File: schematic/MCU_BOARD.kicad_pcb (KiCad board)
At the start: 2 copper layers, 79.2 x 101.1 mm, 83 parts, among them J2 Speaker_Conn_01x02, J3 Barrel_Jack_Switch, J4 Conn_01x27, Q1 2N3904, Q2 2N3904, Q3 2N3904, Q4 2N3904, Q5 2N3904, U5 LM386, U6 74HC4051, U7 AT89S51-24PU, U9 SN74HC4060N, Y1 32.768Khz, Y2 12Mhz

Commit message: bad state, but wanted to document changes to the v1 cap values. Need to fix PCB, it got messed up for some odd reason.
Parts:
- removed H3: MountingHole, MountingHole:MountingHole_3.2mm_M3
- removed J4: Conn_01x27, Connector_PinHeader_2.54mm:PinHeader_1x27_P2.54mm_Vertical
- removed R42, R43: 100R, Resistor_THT:R_Axial_DIN0207_L6.3mm_D2.5mm_P7.62mm_Horizontal
- removed U5: LM386, Package_DIP:DIP-8_W7.62mm_LongPads
- removed U7: AT89S51-24PU, AT89S51-33PU:DIP1556W56P254L5232H483Q40N
- removed U9: SN74HC4060N, Package_DIP:DIP-16_W7.62mm_LongPads
- added H1: MountingHole, MountingHole:MountingHole_3.2mm_M3, F.Cu at (187.8, 36.1)
- added IC1: SN74HC4060N, Package_DIP:DIP-16_W7.62mm_LongPads, F.Cu at (189.5, 45.0)
- added IC2: AT89S51-24PU, AT89S51-33PU:DIP1556W56P254L5232H483Q40N, F.Cu at (147.9, 87.4)
- added J1: Speaker_Conn_01x02, Connector_Molex:Molex_KK-254_AE-6410-02A_1x02_P2.54mm_Vertical, F.Cu at (154.4, 50.9)
- added R1: 4k7, Resistor_THT:R_Axial_DIN0207_L6.3mm_D2.5mm_P7.62mm_Horizontal, F.Cu at (198.9, 70.6)
- added R2: 4k7, Resistor_THT:R_Axial_DIN0207_L6.3mm_D2.5mm_P7.62mm_Horizontal, F.Cu at (171.2, 103.1)
- added U1: LM386, Package_DIP:DIP-8_W7.62mm_LongPads, F.Cu at (142.2, 39.1)
- C1: footprint Capacitor_THT:C_Disc_D4.3mm_W1.9mm_P5.00mm -> Capacitor_THT:C_Disc_D3.0mm_W1.6mm_P2.50mm
- C13: value 4.7uF -> 2uF
- C14: value 47nF -> 47pF; footprint Capacitor_THT:C_Disc_D4.3mm_W1.9mm_P5.00mm -> Capacitor_THT:C_Disc_D3.0mm_W2.0mm_P2.50mm
- C15: value 330uF -> 220uF; footprint Capacitor_THT:CP_Radial_D6.3mm_P2.50mm -> Capacitor_THT:CP_Radial_D10.0mm_P5.00mm_P7.50mm
- C16: value 330uF -> 470uF; footprint Capacitor_THT:CP_Radial_D6.3mm_P2.50mm -> Capacitor_THT:CP_Radial_D10.0mm_P5.00mm_P7.50mm
- C2: value 6-30pF -> 2-5pF; footprint Capacitor_THT:C_Rect_L7.0mm_W6.5mm_P5.00mm -> Capacitor_THT:C_Rect_L10.0mm_W5.0mm_P5.00mm_P7.50mm
- C24: value 10uF -> 2.2uF
- C26: value 18pF -> 10pF
- J2: value Speaker_Conn_01x02 -> Barrel_Jack_Switch; footprint Connector_Molex:Molex_KK-254_AE-6410-02A_1x02_P2.54mm_Vertical -> Connector_BarrelJack:BarrelJack_Horizontal
- J3: value Barrel_Jack_Switch -> Conn_01x27; footprint Connector_BarrelJack:BarrelJack_Horizontal -> Connector_PinHeader_2.54mm:PinHeader_1x27_P2.54mm_Vertical
- R13: value 470R -> 10M
- R14: value 470R -> 270R
- R15: value 10M -> 10K
- R16: value 1K -> 1k
- R17: value 10K -> 8R_OPT; footprint Resistor_THT:R_Axial_DIN0207_L6.3mm_D2.5mm_P7.62mm_Horizontal -> Resistor_THT:R_Axial_DIN0414_L11.9mm_D4.5mm_P15.24mm_Horizontal
- R18: value 1k -> 5K
- R19: value 8R_OPT -> 500R; footprint Resistor_THT:R_Axial_DIN0414_L11.9mm_D4.5mm_P15.24mm_Horizontal -> Resistor_THT:R_Axial_DIN0207_L6.3mm_D2.5mm_P7.62mm_Horizontal
- R20: value 10K -> 270R; footprint Resistor_THT:R_Axial_DIN0207_L6.3mm_D2.5mm_P7.62mm_Horizontal -> Resistor_THT:R_Axial_DIN0207_L6.3mm_D2.5mm_P10.16mm_Horizontal
- R21: value 470R -> 270R; footprint Resistor_THT:R_Axial_DIN0207_L6.3mm_D2.5mm_P7.62mm_Horizontal -> Resistor_THT:R_Axial_DIN0207_L6.3mm_D2.5mm_P10.16mm_Horizontal
- R22, R23, R24, R25: value 1K -> 270R
- R26: value 1K -> 10R; footprint Resistor_THT:R_Axial_DIN0207_L6.3mm_D2.5mm_P10.16mm_Horizontal -> Resistor_THT:R_Axial_DIN0207_L6.3mm_D2.5mm_P7.62mm_Horizontal
- R27: value 1K -> 10K; footprint Resistor_THT:R_Axial_DIN0207_L6.3mm_D2.5mm_P10.16mm_Horizontal -> Resistor_THT:R_Axial_DIN0207_L6.3mm_D2.5mm_P7.62mm_Horizontal
- R28: value 10R -> 1k
- R35: value 10K -> 100R
- R36: value 1k -> 100R
- R6: value 4k7 -> 1k
- R7: value 4k7 -> 1M
- R8: value 1k -> 470R
- R9: value 200k -> 470R
- moved J3 81.4 mm to (124.3, 125.0), turned to 90 degrees
- moved R27 40.5 mm to (221.8, 97.6)
- moved R26 34.5 mm to (215.9, 101.7)
- moved J2 30.6 mm to (124.5, 43.5), turned to -90 degrees
- moved R8 11.4 mm to (191.5, 66.8)
- moved C15 0.09 mm to (142.3, 51.9)
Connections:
- C1 pad 2: Net-(C1-Pad2) -> Net-(IC1-CLKI)
- C10 pad 1: Net-(C10-Pad1) -> Net-(U1-+)
- C20 pad 2: Net-(C20-Pad2) -> Net-(IC1-~{CLKO})
- C3 pad 2: Net-(C3-Pad2) -> Net-(IC1-CLR)
- C4 pad 1: Net-(C4-Pad1) -> Net-(IC2-(RXD)_P3.0)
- C5 pad 1: Net-(C5-Pad1) -> Net-(IC2-(TXD)_P3.1)
- C6 pad 1: Net-(C6-Pad1) -> Net-(IC2-(~{INT0})_P3.2)
- C7 pad 1: Net-(C7-Pad1) -> Net-(IC2-(~{INT1})_P3.3)
- C8 pad 1: Net-(C8-Pad1) -> Net-(IC2-(T0)_P3.4)
- J2 pad 1: GND -> VCC
- J2 pad 2: Net-(J2-Pad2) -> GND
- J3 pad 1: VCC -> /AL
- J3 pad 2: GND -> /B
- J3 pad 3: GND -> /A
- Q1 pad 2: Net-(Q1-Pad2) -> Net-(Q1-B)
- Q1 pad 3: /LED_DISPLAY_BOARD/DL -> /DL
- Q2 pad 2: Net-(Q2-Pad2) -> Net-(Q2-B)
- Q2 pad 3: /LED_DISPLAY_BOARD/TEN_H -> /TEN_H
- Q3 pad 2: Net-(Q3-Pad2) -> Net-(Q3-B)
- Q3 pad 3: /LED_DISPLAY_BOARD/ONE_H -> /ONE_H
- Q4 pad 2: Net-(Q4-Pad2) -> Net-(Q4-B)
- Q4 pad 3: /LED_DISPLAY_BOARD/TEN_M -> /TEN_M
- Q5 pad 2: Net-(Q5-Pad2) -> Net-(Q5-B)
- Q5 pad 3: /LED_DISPLAY_BOARD/ONE_M -> /ONE_M
- R10 pad 1: /LED_DISPLAY_BOARD/HS -> /AS
- R10 pad 2: Net-(C4-Pad1) -> Net-(IC2-(~{INT0})_P3.2)
- R11 pad 1: Net-(C5-Pad1) -> /TS
- R11 pad 2: /LED_DISPLAY_BOARD/MS -> Net-(IC2-(~{INT1})_P3.3)
- R12 pad 1: /LED_DISPLAY_BOARD/AS -> /SAS
- R12 pad 2: Net-(C6-Pad1) -> Net-(IC2-(T0)_P3.4)
- R13 pad 1: /LED_DISPLAY_BOARD/TS -> Net-(IC1-~{CLKO})
- R13 pad 2: Net-(C7-Pad1) -> Net-(IC1-CLKI)
- R14 pad 1: /LED_DISPLAY_BOARD/SAS -> /AL
- R14 pad 2: Net-(C8-Pad1) -> Net-(IC2-(SCK)_P1.7)
- R15 pad 1: Net-(C20-Pad2) -> VCC
- R15 pad 2: Net-(C1-Pad2) -> Net-(IC2-(MISO)_P1.6)
- R16 pad 1: /LED_DISPLAY_BOARD/AL -> Net-(IC2-(MISO)_P1.6)
- R16 pad 2: Net-(R16-Pad2) -> Net-(Q1-B)
- R17 pad 1: VCC -> Net-(J1-Pin_2)
- R17 pad 2: Net-(R17-Pad2) -> Net-(C15-Pad2)
- R18 pad 1: Net-(R17-Pad2) -> Net-(U1-+)
- R18 pad 2: Net-(Q1-Pad2) -> Net-(C13-Pad2)
- R19 pad 1: Net-(J2-Pad2) -> GND
- R19 pad 2: Net-(C15-Pad2) -> Net-(U1-+)
- R20 pad 1: Net-(C10-Pad1) -> /L0
- R20 pad 2: Net-(C13-Pad2) -> Net-(IC2-P1.0)
- R21 pad 1: GND -> /L1
- R21 pad 2: Net-(C10-Pad1) -> Net-(IC2-P1.1)
- R22 pad 1: /LED_DISPLAY_BOARD/L0 -> /L2
- R23 pad 1: /LED_DISPLAY_BOARD/L1 -> /L3
- R24 pad 1: /LED_DISPLAY_BOARD/L2 -> /L4
- R25 pad 1: /LED_DISPLAY_BOARD/L3 -> /L5
- R26 pad 1: /LED_DISPLAY_BOARD/L4 -> Net-(C14-Pad2)
- R26 pad 2: Net-(R26-Pad2) -> GND
- R27 pad 1: /LED_DISPLAY_BOARD/L5 -> Net-(IC2-P2.0_(A8))
- R27 pad 2: Net-(R27-Pad2) -> VCC
- R28 pad 1: Net-(C14-Pad2) -> Net-(IC2-P2.0_(A8))
- R28 pad 2: GND -> Net-(Q5-B)
- R3 pad 1: /LED_DISPLAY_BOARD/HS -> /AS
- R30 pad 2: Net-(Q5-Pad2) -> Net-(Q2-B)
- R32 pad 2: Net-(Q2-Pad2) -> Net-(Q3-B)
- R34 pad 2: Net-(Q3-Pad2) -> Net-(Q4-B)
- R35 pad 1: Net-(R35-Pad1) -> /A
- R36 pad 1: Net-(R35-Pad1) -> /B
- R36 pad 2: Net-(Q4-Pad2) -> VCC
- R37 pad 1: /MCU_BOARD/A -> /C
- R38 pad 1: /MCU_BOARD/B -> /D
- R39 pad 1: /MCU_BOARD/C -> /E
- R4 pad 1: /LED_DISPLAY_BOARD/MS -> /TS
- R40 pad 1: /MCU_BOARD/D -> /F
- R41 pad 1: /MCU_BOARD/E -> /G
- R5 pad 1: /LED_DISPLAY_BOARD/AS -> /SAS
- R6 pad 1: /LED_DISPLAY_BOARD/TS -> Net-(IC1-CLR)
- R6 pad 2: VCC -> GND
- R7 pad 1: /LED_DISPLAY_BOARD/SAS -> Net-(C2-Pad2)
- R7 pad 2: VCC -> Net-(IC1-~{CLKO})
- R8 pad 1: Net-(C3-Pad2) -> /HS
- R8 pad 2: GND -> Net-(IC2-(RXD)_P3.0)
- R9 pad 1: Net-(C2-Pad2) -> Net-(IC2-(TXD)_P3.1)
- R9 pad 2: Net-(C20-Pad2) -> /MS
- U6 pad 1: /MCU_BOARD/Q6 -> /Q6
- U6 pad 12: /MCU_BOARD/Q5 -> /Q5
- U6 pad 14: /MCU_BOARD/Q3 -> /Q3
- U6 pad 15: /MCU_BOARD/Q4 -> /Q4
- U6 pad 2: /MCU_BOARD/Q8 -> /Q8
- U6 pad 4: /MCU_BOARD/Q9 -> /Q9
- U6 pad 5: /MCU_BOARD/Q7 -> /Q7
- Y1 pad 2: Net-(C1-Pad2) -> Net-(IC1-CLKI)
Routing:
- net (no net): track 0.00 -> 349.9 mm
- net /ONE_M: track 0.00 -> 122.9 mm
- net /LED_DISPLAY_BOARD/ONE_M: track 122.9 -> 0.00 mm
- net /TEN_M: track 0.00 -> 111.0 mm
- net /LED_DISPLAY_BOARD/TEN_M: track 111.0 -> 0.00 mm
- net /G: track 0.00 -> 95.5 mm, vias 0 -> 2
- net /ONE_H: track 0.00 -> 77.2 mm
- net /LED_DISPLAY_BOARD/ONE_H: track 77.2 -> 0.00 mm
- net /F: track 0.00 -> 69.2 mm, vias 0 -> 2
- net /Q7: track 0.00 -> 64.5 mm, vias 0 -> 2
- net /MCU_BOARD/Q7: track 64.5 -> 0.00 mm, vias 2 -> 0
- net /Q9: track 0.00 -> 63.9 mm, vias 0 -> 2
- net /MCU_BOARD/Q9: track 63.9 -> 0.00 mm, vias 2 -> 0
- net /MCU_BOARD/G: track 63.0 -> 0.00 mm
- net /TEN_H: track 0.00 -> 61.7 mm
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
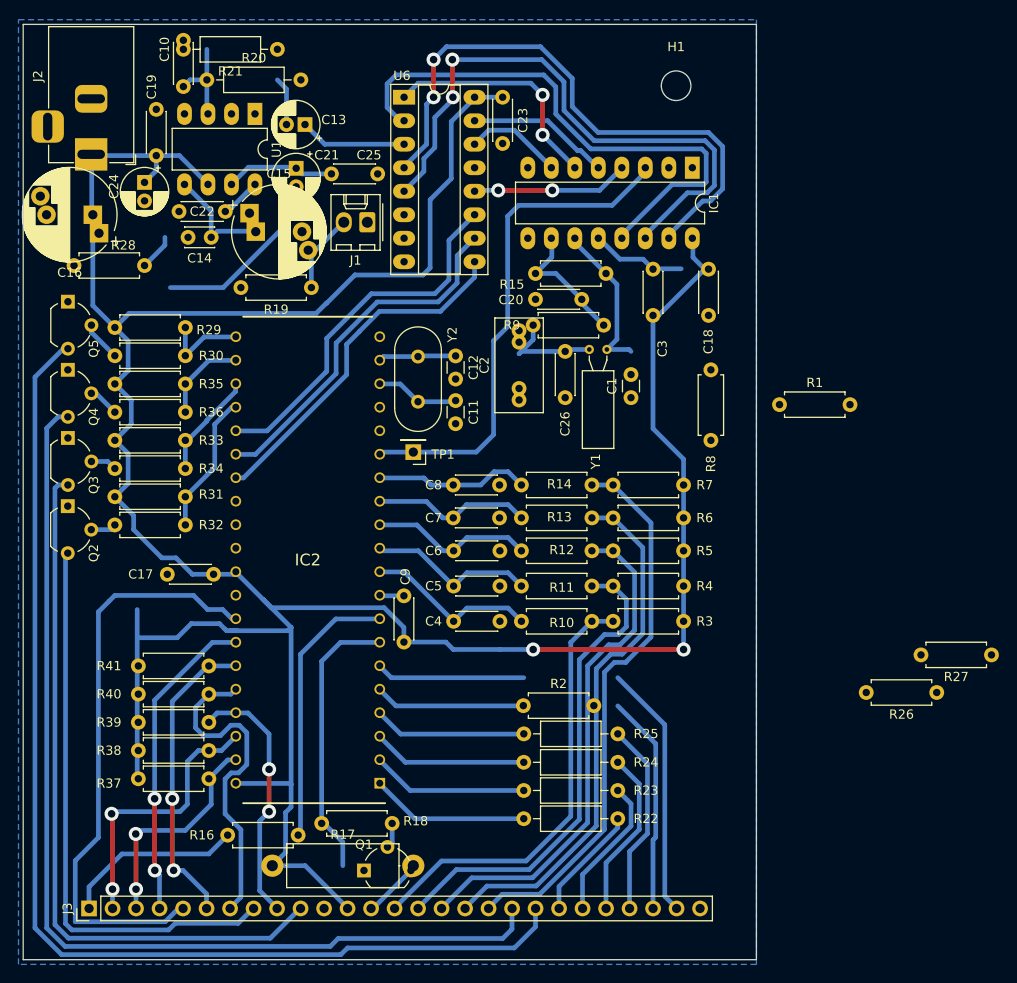
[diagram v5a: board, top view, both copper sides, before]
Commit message: added resistor from input to bypass of lm386. When the alarm is off the input is ground, this reduces noise issues to about nothing. Updated PCB.
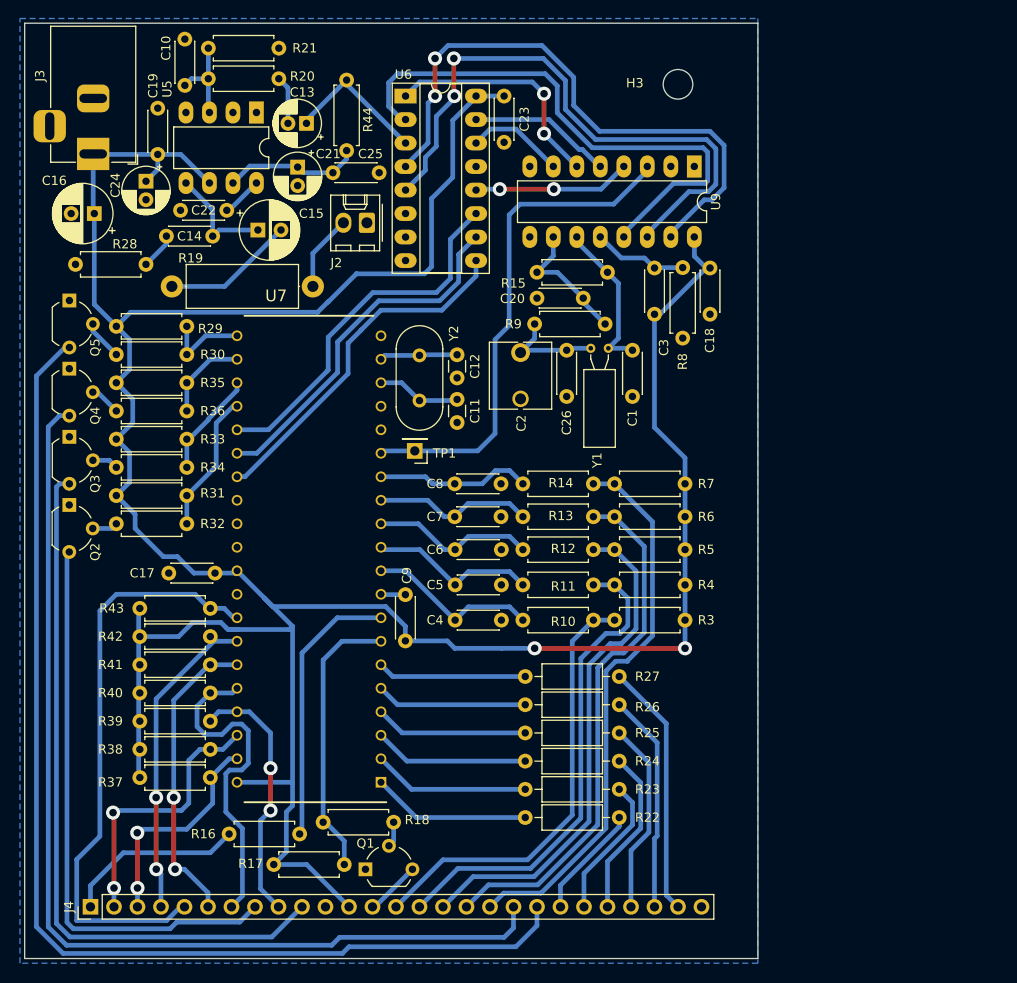
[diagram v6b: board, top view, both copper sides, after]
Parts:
- removed H1: MountingHole, MountingHole:MountingHole_3.2mm_M3
- removed IC1: SN74HC4060N, Package_DIP:DIP-16_W7.62mm_LongPads
- removed IC2: AT89S51-24PU, AT89S51-33PU:DIP1556W56P254L5232H483Q40N
- removed J1: Speaker_Conn_01x02, Connector_Molex:Molex_KK-254_AE-6410-02A_1x02_P2.54mm_Vertical
- removed R1, R2: 4k7, Resistor_THT:R_Axial_DIN0207_L6.3mm_D2.5mm_P7.62mm_Horizontal
- removed U1: LM386, Package_DIP:DIP-8_W7.62mm_LongPads
- added H3: MountingHole, MountingHole:MountingHole_3.2mm_M3, F.Cu at (188.0, 35.9)
- added J4: Conn_01x27, Connector_PinHeader_2.54mm:PinHeader_1x27_P2.54mm_Vertical, F.Cu at (124.5, 124.8)
- added R42: 100R, Resistor_THT:R_Axial_DIN0207_L6.3mm_D2.5mm_P7.62mm_Horizontal, F.Cu at (137.4, 95.6)
- added R43: 100R, Resistor_THT:R_Axial_DIN0207_L6.3mm_D2.5mm_P7.62mm_Horizontal, F.Cu at (137.4, 92.6)
- added R44: 470R, Resistor_THT:R_Axial_DIN0207_L6.3mm_D2.5mm_P7.62mm_Horizontal, F.Cu at (152.1, 43.1)
- added U5: LM386, Package_DIP:DIP-8_W7.62mm_LongPads, F.Cu at (142.4, 39.0)
- added U7: AT89S51-24PU, AT89S51-33PU:DIP1556W56P254L5232H483Q40N, F.Cu at (148.1, 87.2)
- added U9: SN74HC4060N, Package_DIP:DIP-16_W7.62mm_LongPads, F.Cu at (189.7, 44.8)
- C1: footprint Capacitor_THT:C_Disc_D3.0mm_W1.6mm_P2.50mm -> Capacitor_THT:C_Disc_D4.3mm_W1.9mm_P5.00mm
- C13: value 2uF -> 4.7uF
- C14: value 47pF -> 47nF; footprint Capacitor_THT:C_Disc_D3.0mm_W2.0mm_P2.50mm -> Capacitor_THT:C_Disc_D4.3mm_W1.9mm_P5.00mm
- C15: value 220uF -> 330uF; footprint Capacitor_THT:CP_Radial_D10.0mm_P5.00mm_P7.50mm -> Capacitor_THT:CP_Radial_D6.3mm_P2.50mm
- C16: value 470uF -> 330uF; footprint Capacitor_THT:CP_Radial_D10.0mm_P5.00mm_P7.50mm -> Capacitor_THT:CP_Radial_D6.3mm_P2.50mm
- C2: footprint Capacitor_THT:C_Rect_L10.0mm_W5.0mm_P5.00mm_P7.50mm -> Capacitor_THT:C_Rect_L7.0mm_W6.5mm_P5.00mm
- C24: value 2.2uF -> 10uF
- C26: value 10pF -> 8pF
- J2: value Barrel_Jack_Switch -> Speaker_Conn_01x02; footprint Connector_BarrelJack:BarrelJack_Horizontal -> Connector_Molex:Molex_KK-254_AE-6410-02A_1x02_P2.54mm_Vertical
- J3: value Conn_01x27 -> Barrel_Jack_Switch; footprint Connector_PinHeader_2.54mm:PinHeader_1x27_P2.54mm_Vertical -> Connector_BarrelJack:BarrelJack_Horizontal
- R13: value 10M -> 470R
- R14: value 270R -> 470R
- R15: value 10K -> 10M
- R16: value 1k -> 1K
- R17: value 8R_OPT -> 10K; footprint Resistor_THT:R_Axial_DIN0414_L11.9mm_D4.5mm_P15.24mm_Horizontal -> Resistor_THT:R_Axial_DIN0207_L6.3mm_D2.5mm_P7.62mm_Horizontal
- R18: value 5K -> 1k
- R19: value 500R -> 8R_OPT; footprint Resistor_THT:R_Axial_DIN0207_L6.3mm_D2.5mm_P7.62mm_Horizontal -> Resistor_THT:R_Axial_DIN0414_L11.9mm_D4.5mm_P15.24mm_Horizontal
- R20: value 270R -> 10K; footprint Resistor_THT:R_Axial_DIN0207_L6.3mm_D2.5mm_P10.16mm_Horizontal -> Resistor_THT:R_Axial_DIN0207_L6.3mm_D2.5mm_P7.62mm_Horizontal
- R21: value 270R -> 470R; footprint Resistor_THT:R_Axial_DIN0207_L6.3mm_D2.5mm_P10.16mm_Horizontal -> Resistor_THT:R_Axial_DIN0207_L6.3mm_D2.5mm_P7.62mm_Horizontal
- R22, R23, R24, R25: value 270R -> 1K
- R26: value 10R -> 1K; footprint Resistor_THT:R_Axial_DIN0207_L6.3mm_D2.5mm_P7.62mm_Horizontal -> Resistor_THT:R_Axial_DIN0207_L6.3mm_D2.5mm_P10.16mm_Horizontal
- R27: value 10K -> 1K; footprint Resistor_THT:R_Axial_DIN0207_L6.3mm_D2.5mm_P7.62mm_Horizontal -> Resistor_THT:R_Axial_DIN0207_L6.3mm_D2.5mm_P10.16mm_Horizontal
- R28: value 1k -> 10R
- R35: value 100R -> 10K
- R36: value 100R -> 1k
- R6: value 1k -> 4k7
- R7: value 1M -> 4k7
- R8: value 470R -> 1k
- R9: value 470R -> 200k
- moved J3 81.6 mm to (124.8, 43.5), turned to -90 degrees
- moved R27 40.3 mm to (181.6, 99.9)
- moved R26 34.3 mm to (181.6, 103.0)
- moved J2 30.7 mm to (154.3, 50.9), turned to 180 degrees
- moved R8 11.5 mm to (188.5, 55.8)
- moved C15 0.29 mm to (142.6, 51.7)
- moved C8 0.20 mm to (163.8, 79.1)
- moved R22 0.20 mm to (181.6, 115.2)
- moved R9 0.20 mm to (172.5, 61.8)
- moved U6 0.20 mm to (158.5, 37.2)
- moved C10 0.20 mm to (134.7, 36.1)
- moved C2 0.20 mm to (170.9, 69.9)
- moved C24 0.20 mm to (130.5, 46.4)
- moved C7 0.20 mm to (163.8, 82.7)
- moved C9 0.20 mm to (158.5, 96.1)
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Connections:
- C1 pad 2: Net-(IC1-CLKI) -> (no net)
- C10 pad 1: Net-(U1-+) -> (no net)
- C11 pad 2: Net-(IC2-XTAL2) -> (no net)
- C12 pad 1: Net-(IC2-XTAL1) -> (no net)
- C20 pad 2: Net-(IC1-~{CLKO}) -> (no net)
- C21 pad 1: Net-(U1-BYPASS) -> (no net)
- C25 pad 1: Net-(U1-BYPASS) -> (no net)
- C3 pad 2: Net-(IC1-CLR) -> (no net)
- C4 pad 1: Net-(IC2-(RXD)_P3.0) -> (no net)
- C5 pad 1: Net-(IC2-(TXD)_P3.1) -> (no net)
- C6 pad 1: Net-(IC2-(~{INT0})_P3.2) -> (no net)
- C7 pad 1: Net-(IC2-(~{INT1})_P3.3) -> (no net)
- C8 pad 1: Net-(IC2-(T0)_P3.4) -> (no net)
- C9 pad 2: Net-(IC2-RST) -> (no net)
- J2 pad 1: VCC -> GND
- J2 pad 2: GND -> (no net)
- J3 pad 1: /AL -> VCC
- J3 pad 2: /B -> GND
- J3 pad 3: /A -> GND
- Q1 pad 3: /DL -> (no net)
- Q2 pad 3: /TEN_H -> (no net)
- Q3 pad 3: /ONE_H -> (no net)
- Q4 pad 3: /TEN_M -> (no net)
- Q5 pad 3: /ONE_M -> (no net)
- R10 pad 1: /AS -> (no net)
- R10 pad 2: Net-(IC2-(~{INT0})_P3.2) -> (no net)
- R11 pad 1: /TS -> (no net)
- R11 pad 2: Net-(IC2-(~{INT1})_P3.3) -> (no net)
- R12 pad 1: /SAS -> (no net)
- R12 pad 2: Net-(IC2-(T0)_P3.4) -> (no net)
- R13 pad 1: Net-(IC1-~{CLKO}) -> (no net)
- R13 pad 2: Net-(IC1-CLKI) -> (no net)
- R14 pad 1: /AL -> (no net)
- R14 pad 2: Net-(IC2-(SCK)_P1.7) -> (no net)
- R15 pad 1: VCC -> (no net)
- R15 pad 2: Net-(IC2-(MISO)_P1.6) -> (no net)
- R16 pad 1: Net-(IC2-(MISO)_P1.6) -> (no net)
- R16 pad 2: Net-(Q1-B) -> (no net)
- R17 pad 1: Net-(J1-Pin_2) -> VCC
- R17 pad 2: Net-(C15-Pad2) -> (no net)
- R18 pad 1: Net-(U1-+) -> (no net)
- R18 pad 2: Net-(C13-Pad2) -> Net-(Q1-B)
- R19 pad 1: GND -> (no net)
- R19 pad 2: Net-(U1-+) -> Net-(C15-Pad2)
- R20 pad 1: /L0 -> (no net)
- R20 pad 2: Net-(IC2-P1.0) -> Net-(C13-Pad2)
- R21 pad 1: /L1 -> GND
- R21 pad 2: Net-(IC2-P1.1) -> (no net)
- R22 pad 1: /L2 -> (no net)
- R22 pad 2: Net-(IC2-P1.2) -> (no net)
- R23 pad 1: /L3 -> (no net)
- R23 pad 2: Net-(IC2-P1.3) -> (no net)
- R24 pad 1: /L4 -> (no net)
- R24 pad 2: Net-(IC2-P1.4) -> (no net)
- R25 pad 1: /L5 -> (no net)
- R25 pad 2: Net-(IC2-(MOSI)_P1.5) -> (no net)
- R26 pad 1: Net-(C14-Pad2) -> (no net)
- R26 pad 2: GND -> (no net)
- R27 pad 1: Net-(IC2-P2.0_(A8)) -> (no net)
- R27 pad 2: VCC -> (no net)
- R28 pad 1: Net-(IC2-P2.0_(A8)) -> Net-(C14-Pad2)
- R28 pad 2: Net-(Q5-B) -> GND
- R29 pad 1: Net-(IC2-P2.3_(A11)) -> (no net)
- R3 pad 1: /AS -> (no net)
- R30 pad 1: Net-(IC2-P2.3_(A11)) -> (no net)
- R30 pad 2: Net-(Q2-B) -> Net-(Q5-B)
- R31 pad 1: Net-(IC2-P2.2_(A10)) -> (no net)
- R32 pad 1: Net-(IC2-P2.2_(A10)) -> (no net)
- R32 pad 2: Net-(Q3-B) -> Net-(Q2-B)
- R33 pad 1: Net-(IC2-P2.1_(A9)) -> (no net)
- R34 pad 1: Net-(IC2-P2.1_(A9)) -> (no net)
- R34 pad 2: Net-(Q4-B) -> Net-(Q3-B)
- R35 pad 1: /A -> (no net)
- R36 pad 1: /B -> (no net)
- R36 pad 2: VCC -> Net-(Q4-B)
- R37 pad 1: /C -> (no net)
- R38 pad 1: /D -> (no net)
- R39 pad 1: /E -> (no net)
- R4 pad 1: /TS -> (no net)
- R40 pad 1: /F -> (no net)
- R41 pad 1: /G -> (no net)
- R5 pad 1: /SAS -> (no net)
- R6 pad 1: Net-(IC1-CLR) -> (no net)
- R6 pad 2: GND -> VCC
- R7 pad 1: Net-(C2-Pad2) -> (no net)
- R7 pad 2: Net-(IC1-~{CLKO}) -> VCC
- R8 pad 1: /HS -> (no net)
- R8 pad 2: Net-(IC2-(RXD)_P3.0) -> GND
- R9 pad 1: Net-(IC2-(TXD)_P3.1) -> Net-(C2-Pad2)
- R9 pad 2: /MS -> (no net)
- TP1 pad 1: Net-(IC1-QN) -> (no net)
- U6 pad 1: /Q6 -> (no net)
- U6 pad 10: Net-(IC2-P2.5_(A13)) -> (no net)
- U6 pad 11: Net-(IC2-P2.4_(A12)) -> (no net)
- U6 pad 12: /Q5 -> (no net)
- U6 pad 14: /Q3 -> (no net)
- U6 pad 15: /Q4 -> (no net)
- U6 pad 2: /Q8 -> (no net)
- U6 pad 4: /Q9 -> (no net)
- U6 pad 5: /Q7 -> (no net)
- U6 pad 9: Net-(IC2-P2.6_(A14)) -> (no net)
- Y1 pad 2: Net-(IC1-CLKI) -> (no net)
- Y2 pad 1: Net-(IC2-XTAL1) -> (no net)
- Y2 pad 2: Net-(IC2-XTAL2) -> (no net)
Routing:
- net (no net): track 349.9 -> 1855.6 mm, vias 0 -> 18
- net /ONE_M: track 122.9 -> 0.00 mm
- net /TEN_M: track 111.0 -> 0.00 mm
- net /G: track 95.5 -> 0.00 mm, vias 2 -> 0
- net /ONE_H: track 77.2 -> 0.00 mm
- net /F: track 69.2 -> 0.00 mm, vias 2 -> 0
- net /Q7: track 64.5 -> 0.00 mm, vias 2 -> 0
- net /Q9: track 63.9 -> 0.00 mm, vias 2 -> 0
- net /TEN_H: track 61.7 -> 0.00 mm
- net /Q8: track 60.0 -> 0.00 mm
- net /SAS: track 55.1 -> 0.00 mm
- net Net-(IC1-QN): track 54.8 -> 0.00 mm
- net /L5: track 48.5 -> 0.00 mm
- net /AS: track 47.5 -> 0.00 mm
- net /L4: track 41.9 -> 0.00 mm
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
